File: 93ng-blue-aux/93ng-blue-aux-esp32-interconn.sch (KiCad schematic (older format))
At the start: 39 parts, among them J1 12V INPUT, J2 ESP32 UART, J3 USB_C_Receptacle_USB2.0, J4 Conn_02x16_Row_Letter_First, J7 I-BUS, Q1 S8050, Q2 S8050, SW1 PWR IN SELECT, U1 ESP32-WROOM-32D, U2 NCP1117-3.3_SOT223, U3 MC33897, U5 CP2102N-A01-GQFN28

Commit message: Working on saab board interconnect
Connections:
- net 3.3V: now also J4.a3 (Pin_a3)
- net GND: now also J4.a2 (Pin_a2), J4.a4 (Pin_a4)
- net ESP32_10: now reaches U1.10 (IO25)
- net ESP32_11: now reaches U1.11 (IO26)
- net ESP32_12: now reaches U1.12 (IO27)
- net ESP32_13: now reaches U1.13 (IO14)
- net ESP32_14: now reaches U1.14 (IO12)
- net ESP32_16: now reaches U1.16 (IO13)
- net ESP32_17: now reaches U1.17 (SHD/SD2)
- net ESP32_18: now reaches U1.18 (SWP/SD3)
- net ESP32_19: now reaches U1.19 (SCS/CMD)
- net ESP32_20: now reaches U1.20 (SCK/CLK)
- net ESP32_21: now reaches U1.21 (SDO/SD0)
- net ESP32_22: now reaches U1.22 (SDI/SD1)
- net ESP32_23: now reaches U1.23 (IO15)
- net ESP32_26: now reaches U1.26 (IO4)
- net ESP32_29: now reaches U1.29 (IO5)
- net ESP32_33: now reaches U1.33 (IO21)
- net ESP32_36: now reaches U1.36 (IO22)
- net ESP32_37: now reaches U1.37 (IO23)
- net ESP32_6: now reaches U1.6 (IO34)
- net ESP32_7: now reaches U1.7 (IO35)
- net ESP32_8: now reaches U1.8 (IO32)
- net ESP32_9: now reaches U1.9 (IO33)
- net V_IN: now reaches C1.1, SW1.2 (B), U2.3 (VI)
- net V_IN: now also J4.a1 (Pin_a1)
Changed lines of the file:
@@
 	0    1    1    0
 $EndComp
+Text GLabel 1550 4600 0    50   Input ~ 0
+ESP32_21
+Text GLabel 1550 4700 0    50   Input ~ 0
+ESP32_22
+Text GLabel 1550 4800 0    50   Input ~ 0
+ESP32_17
+Text GLabel 1550 4900 0    50   Input ~ 0
+ESP32_18
+Text GLabel 1550 5000 0    50   Input ~ 0
+ESP32_20
+Text GLabel 1550 5100 0    50   Input ~ 0
+ESP32_19
+Text GLabel 2750 3800 2    50   Input ~ 0
+ESP32_26
+Text GLabel 2750 3900 2    50   Input ~ 0
+ESP32_29
+Text GLabel 2750 4000 2    50   Input ~ 0
+ESP32_14
+Text GLabel 2750 4100 2    50   Input ~ 0
+ESP32_16
+Text GLabel 2750 4200 2    50   Input ~ 0
+ESP32_13
+Text GLabel 2750 4300 2    50   Input ~ 0
+ESP32_23
+Text GLabel 2750 4800 2    50   Input ~ 0
+ESP32_33
+Text GLabel 2750 4900 2    50   Input ~ 0
+ESP32_36
+Text GLabel 2750 5000 2    50   Input ~ 0
+ESP32_37
+Text GLabel 2750 5100 2    50   Input ~ 0
+ESP32_10
+Text GLabel 2750 5200 2    50   Input ~ 0
+ESP32_11
+Text GLabel 2750 5300 2    50   Input ~ 0
+ESP32_12
+Text GLabel 2750 5400 2    50   Input ~ 0
+ESP32_8
+Text GLabel 2750 5500 2    50   Input ~ 0
+ESP32_9
+Text GLabel 2750 5600 2    50   Input ~ 0
+ESP32_6
+Text GLabel 2750 5700 2    50   Input ~ 0
+ESP32_7
+Text GLabel 3250 6450 1    50   Input ~ 0
+GND
+Text GLabel 3350 6450 1    50   Input ~ 0
+3.3V
+Text GLabel 2150 2250 1    50   Input ~ 0
+V_IN
+Text GLabel 3450 6450 1    50   Input ~ 0
+GND
+Text GLabel 3550 6450 1    50   Input ~ 0
+V_IN
 $EndSCHEMATC

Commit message: I forget what I did.
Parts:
- J4: symbol Connector_Generic:Conn_02x16_Row_Letter_First -> Connector_Generic:Conn_02x16_Top_Bottom
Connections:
- net 3.3V: now also J4.3 (Pin_3); no longer J4.a3 (Pin_a3)
- net ESP32_10: now also J4.13 (Pin_13)
- net ESP32_11: now also J4.14 (Pin_14)
- net ESP32_12: now also J4.15 (Pin_15)
- net ESP32_13: now also J4.16 (Pin_16)
- net ESP32_14: now also J4.17 (Pin_17)
- net ESP32_16: now also J4.18 (Pin_18)
- net ESP32_17: now also J4.19 (Pin_19)
- net ESP32_18: now also J4.20 (Pin_20)
- net ESP32_19: now also J4.21 (Pin_21)
- net ESP32_20: now also J4.22 (Pin_22)
- net ESP32_21: now also J4.23 (Pin_23)
- net ESP32_22: now also J4.24 (Pin_24)
- net ESP32_23: now also J4.25 (Pin_25)
- net ESP32_26: now also J4.26 (Pin_26)
- net ESP32_29: now also J4.27 (Pin_27)
- net ESP32_33: now also J4.28 (Pin_28)
- net ESP32_36: now also J4.29 (Pin_29)
- net ESP32_37: now also J4.30 (Pin_30)
- net ESP32_6: now also J4.9 (Pin_9)
- net ESP32_7: now also J4.10 (Pin_10)
- net ESP32_8: now also J4.11 (Pin_11)
- net ESP32_9: now also J4.12 (Pin_12)
- net GND: now also J4.2 (Pin_2), J4.4 (Pin_4); no longer J4.a2 (Pin_a2), J4.a4 (Pin_a4)
- net MC33_MODE0: now also J4.7 (Pin_7)
- net MC33_MODE1: now also J4.8 (Pin_8)
- net MC33_RX: now also J4.5 (Pin_5)
- net MC33_TX: now also J4.6 (Pin_6)
- net V_IN: now also J4.1 (Pin_1); no longer J4.a1 (Pin_a1)
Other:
- moved on the sheet: J4
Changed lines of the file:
@@
 $EndComp
 $Comp
-L Connector_Generic:Conn_02x16_Row_Letter_First J4
+L Connector_Generic:Conn_02x16_Top_Bottom J4
 U 1 1 5E57890B
-P 2850 6650
-F 0 "J4" V 2854 5762 50  0000 R CNN
-F 1 "Conn_02x16_Row_Letter_First" V 2945 5762 50  0000 R CNN
-F 2 "Connector_PinHeader_1.00mm:PinHeader_2x16_P1.00mm_Vertical" H 2850 6650 50  0001 C CNN
-F 3 "~" H 2850 6650 50  0001 C CNN
-	1    2850 6650
+P 2850 6950
+F 0 "J4" V 2854 6062 50  0000 R CNN
+F 1 "Conn_02x16_Row_Letter_First" V 2945 6062 50  0000 R CNN
+F 2 "Connector_PinHeader_1.00mm:PinHeader_2x16_P1.00mm_Vertical" H 2850 6950 50  0001 C CNN
+F 3 "~" H 2850 6950 50  0001 C CNN
+	1    2850 6950
 	0    1    1    0
 $EndComp
@@
 Text GLabel 2750 4800 2    50   Input ~ 0
 ESP32_33
-Text GLabel 2750 4900 2    50   Input ~ 0
-ESP32_36
 Text GLabel 2750 5000 2    50   Input ~ 0
 ESP32_37
@@
 Text GLabel 2750 5700 2    50   Input ~ 0
 ESP32_7
-Text GLabel 3250 6450 1    50   Input ~ 0
+Text GLabel 3250 6750 1    50   Input ~ 0
 GND
-Text GLabel 3350 6450 1    50   Input ~ 0
+Text GLabel 3350 6750 1    50   Input ~ 0
 3.3V
 Text GLabel 2150 2250 1    50   Input ~ 0
 V_IN
-Text GLabel 3450 6450 1    50   Input ~ 0
+Text GLabel 3450 6750 1    50   Input ~ 0
 GND
-Text GLabel 3550 6450 1    50   Input ~ 0
+Text GLabel 3550 6750 1    50   Input ~ 0
 V_IN
+Text GLabel 3150 6750 1    50   Input ~ 0
+MC33_RX
+Text GLabel 3050 6750 1    50   Input ~ 0
+MC33_TX
+Text GLabel 2950 6750 1    50   Input ~ 0
+MC33_MODE0
+Text GLabel 2850 6750 1    50   Input ~ 0
+MC33_MODE1
+Text GLabel 2750 6750 1    50   Input ~ 0
+ESP32_6
+Text GLabel 2650 6750 1    50   Input ~ 0
+ESP32_7
+Text GLabel 2550 6750 1    50   Input ~ 0
+ESP32_8
+Text GLabel 2450 6750 1    50   Input ~ 0
+ESP32_9
+Text GLabel 2350 6750 1    50   Input ~ 0
+ESP32_10
+Text GLabel 2250 6750 1    50   Input ~ 0
+ESP32_11
+Text GLabel 2150 6750 1    50   Input ~ 0
+ESP32_12
+Text GLabel 2050 6750 1    50   Input ~ 0
+ESP32_13
+Text GLabel 3550 7250 3    50   Input ~ 0
+ESP32_14
+Text GLabel 3450 7250 3    50   Input ~ 0
+ESP32_16
+Text GLabel 3350 7250 3    50   Input ~ 0
+ESP32_17
+Text GLabel 3250 7250 3    50   Input ~ 0
+ESP32_18
+Text GLabel 3150 7250 3    50   Input ~ 0
+ESP32_19
+Text GLabel 3050 7250 3    50   Input ~ 0
+ESP32_20
+Text GLabel 2950 7250 3    50   Input ~ 0
+ESP32_21
+Text GLabel 2850 7250 3    50   Input ~ 0
+ESP32_22
+Text GLabel 2750 7250 3    50   Input ~ 0
+ESP32_23
+Text GLabel 2650 7250 3    50   Input ~ 0
+ESP32_26
+Text GLabel 2550 7250 3    50   Input ~ 0
+ESP32_29
+Text GLabel 2450 7250 3    50   Input ~ 0
+ESP32_33
+Text GLabel 2750 4900 2    50   Input ~ 0
+ESP32_36
+Text GLabel 2350 7250 3    50   Input ~ 0
+ESP32_36
+Text GLabel 2250 7250 3    50   Input ~ 0
+ESP32_37
 $EndSCHEMATC

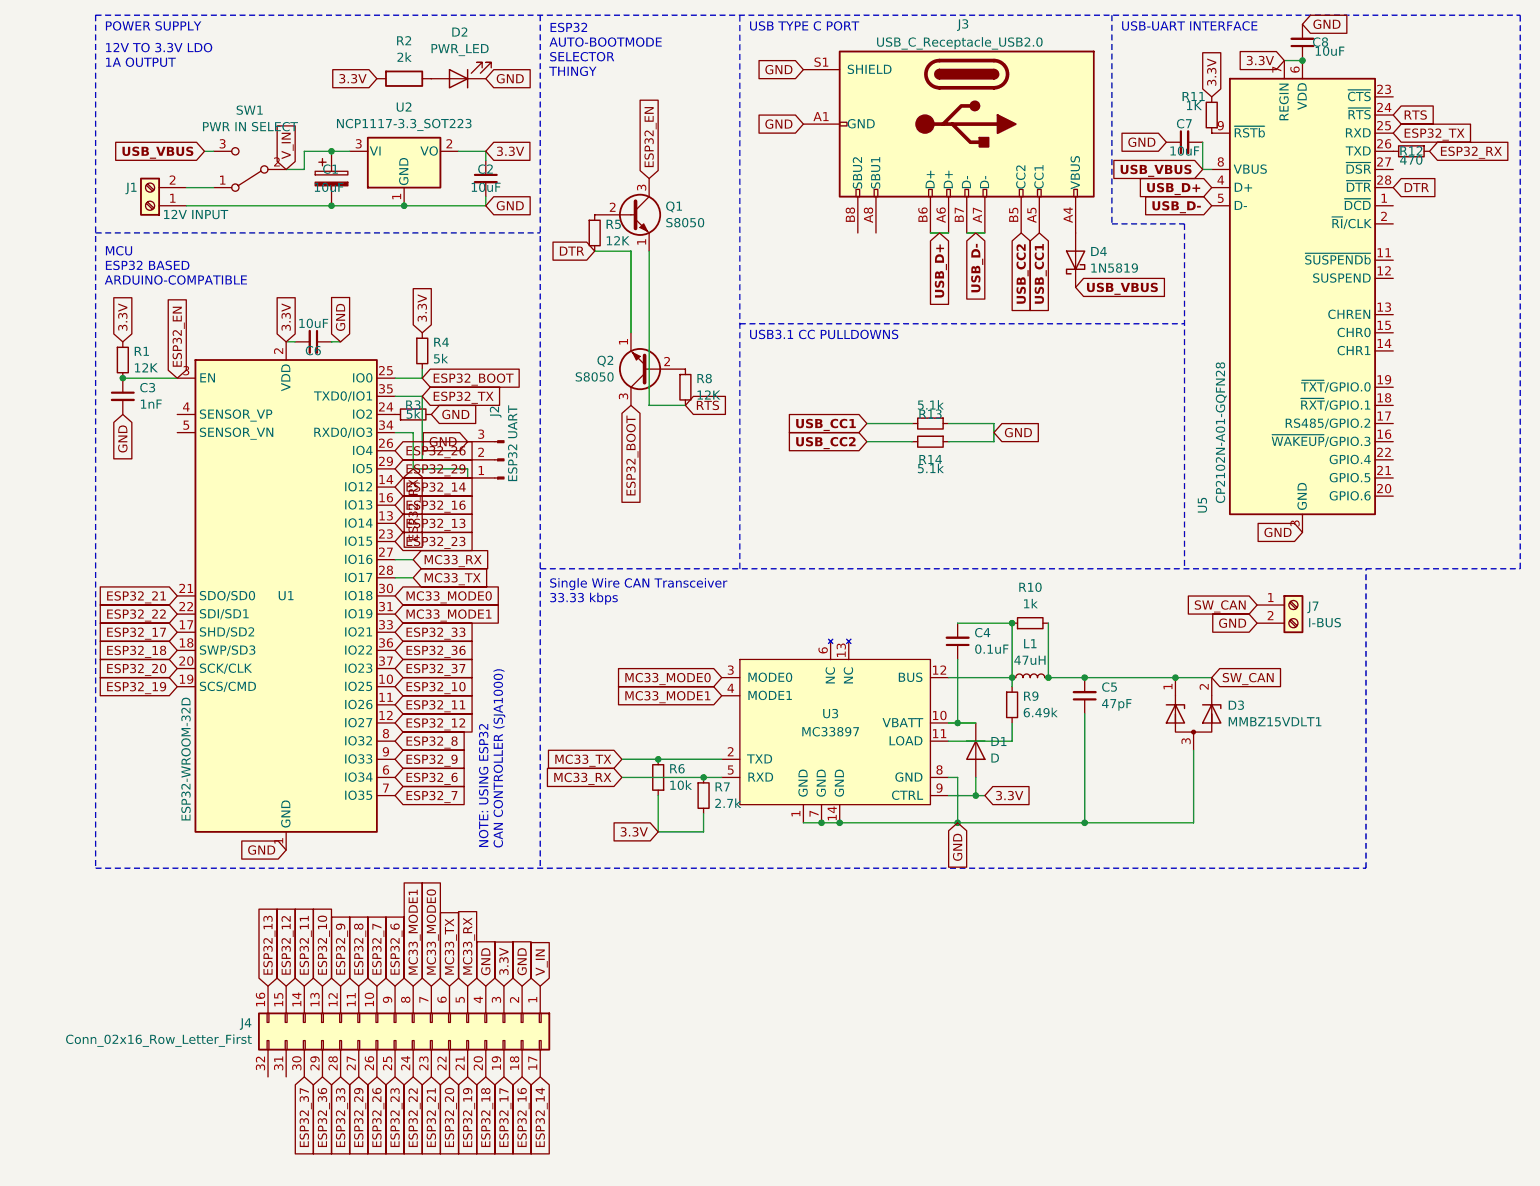
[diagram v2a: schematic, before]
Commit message: Completed first draft of final ESP32 board design, with autorouting
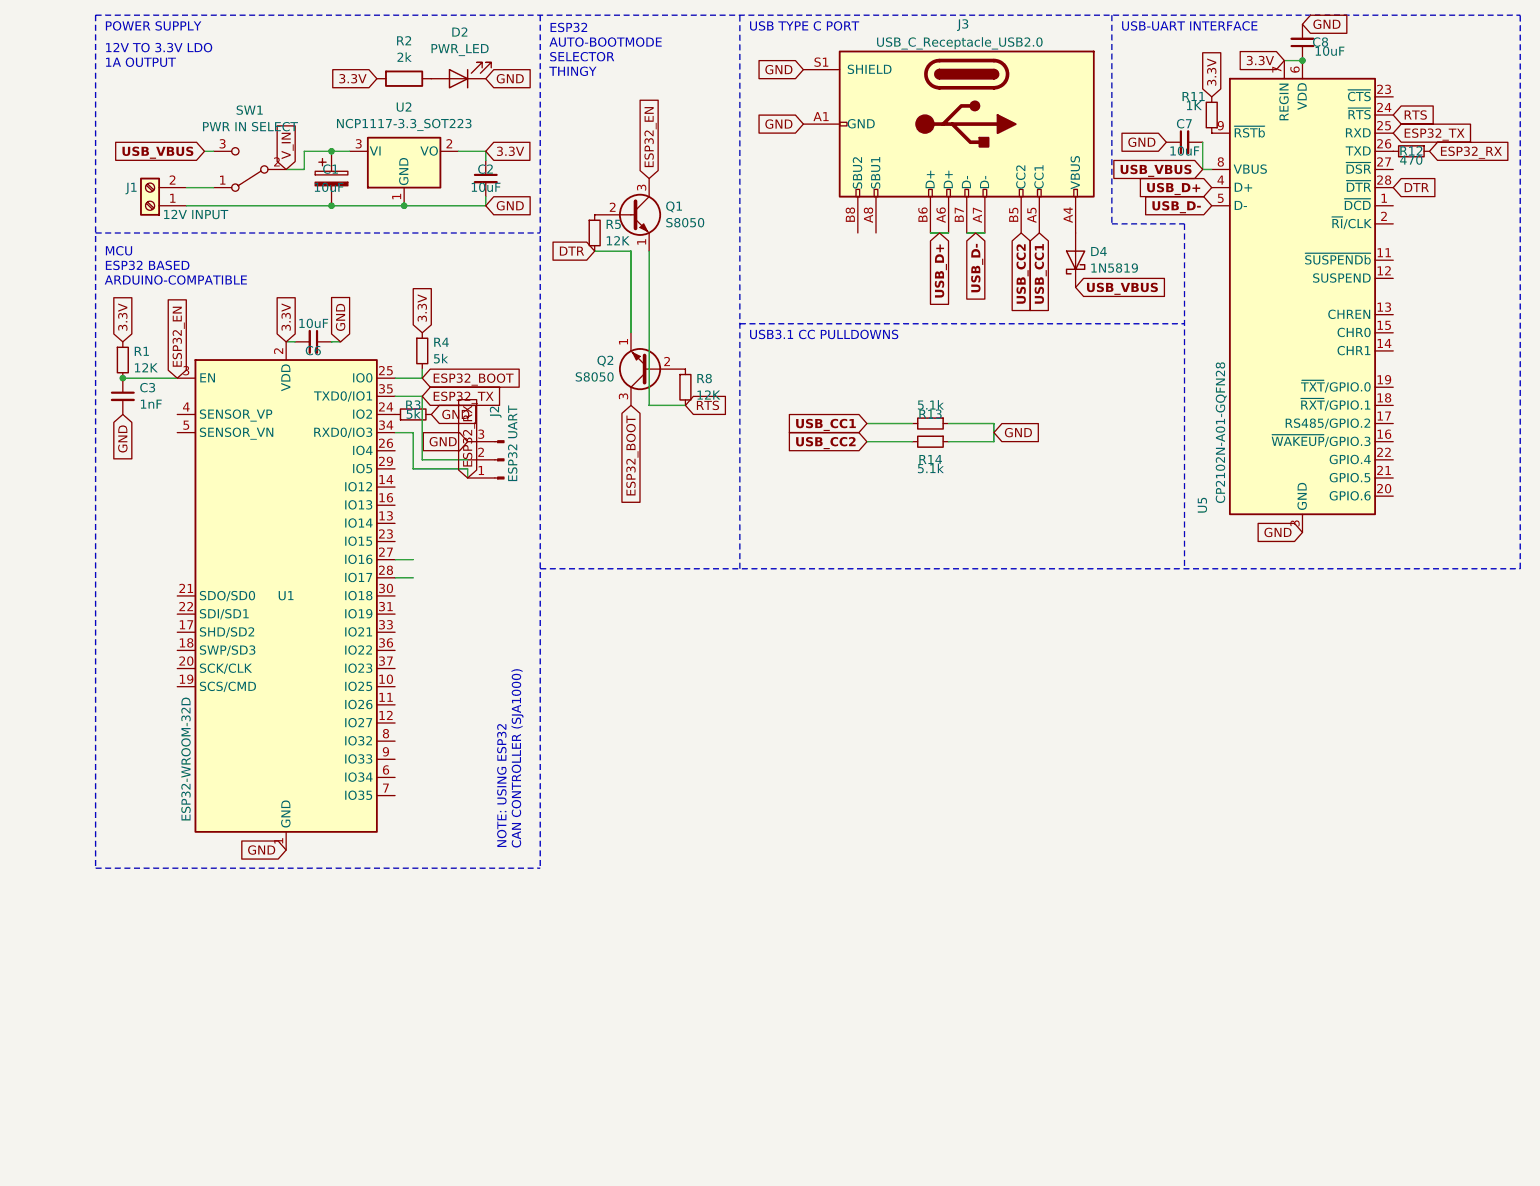
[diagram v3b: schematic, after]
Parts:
- removed C4: 0.1uF, Capacitor_SMD:C_0805_2012Metric_Pad1.15x1.40mm_HandSolder, symbol Device:C_Small
- removed C5: 47pF, Capacitor_SMD:C_0805_2012Metric_Pad1.15x1.40mm_HandSolder, symbol Device:C_Small
- removed D1: D, Diode_SMD:D_0805_2012Metric_Pad1.15x1.40mm_HandSolder, symbol Device:D
- removed D3: MMBZ15VDLT1, Package_TO_SOT_SMD:SOT-23, symbol Diode:MMBZxx
- removed J4: Conn_02x16_Row_Letter_First, Connector_PinHeader_1.00mm:PinHeader_2x16_P1.00mm_Vertical, symbol Connector_Generic:Conn_02x16_Top_Bottom
- removed J7: I-BUS, TerminalBlock_Phoenix:TerminalBlock_Phoenix_MKDS-3-2-5.08_1x02_P5.08mm_Horizontal, symbol Connector:Screw_Terminal_01x02
- removed L1: 47uH, Inductor_SMD:L_0805_2012Metric_Pad1.15x1.40mm_HandSolder, symbol Device:L_Small
- removed R10: 1k, Resistor_SMD:R_0805_2012Metric_Pad1.15x1.40mm_HandSolder, symbol Device:R_Small
- removed R6: 10k, Resistor_SMD:R_0805_2012Metric_Pad1.15x1.40mm_HandSolder, symbol Device:R_Small
- removed R7: 2.7k, Resistor_SMD:R_0805_2012Metric_Pad1.15x1.40mm_HandSolder, symbol Device:R_Small
- removed R9: 6.49k, Resistor_SMD:R_0805_2012Metric_Pad1.15x1.40mm_HandSolder, symbol Device:R_Small
- removed U3: MC33897, Package_SO:SOIC-14_3.9x8.7mm_P1.27mm, symbol custom_symbols:MC33897
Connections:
- net labels removed: ESP32_10, ESP32_11, ESP32_12, ESP32_13, ESP32_14, ESP32_16, ESP32_17, ESP32_18, ESP32_19, ESP32_20, ESP32_21, ESP32_22, ESP32_23, ESP32_26, ESP32_29, ESP32_33, ESP32_36, ESP32_37, ESP32_6, ESP32_7, ESP32_8, ESP32_9, MC33_MODE0, MC33_MODE1, MC33_RX, MC33_TX, SW_CAN
- wire segments 72 -> 40
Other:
- note removed: "Single Wire CAN Transceiver\n33.33 kbps"
